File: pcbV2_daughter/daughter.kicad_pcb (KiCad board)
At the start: 2 copper layers, 93.7 x 93.3 mm, 80 parts, among them J1 Conn_01x02_Female, J2 USB_C_Receptacle, J3 Conn_01x03_Male, J6 Conn_01x03_Male, Q1 Q_NMOS_GSD, SW1 SW_Push, SW10 SW_Push, SW11 SW_Push, SW12 SW_Push, SW13 SW_SPDT, SW14 SW_Push, SW15 SW_Push, SW16 SW_Push, SW17 SW_DIP_x03, SW2 SW_Push, SW3 SW_Push, SW4 SW_Push, SW5 SW_Push, SW6 SW_Push, SW7 SW_Push, SW8 SW_Push, SW9 SW_Push, U1 Teensy4.0, U2 Waveshare_OLED_RGB

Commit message: finished v1 of daughter board
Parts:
- removed C13, C14, C15, C16: 1000uF, Capacitor_SMD:C_1206_3216Metric_Pad1.42x1.75mm_HandSolder
- removed D1, D10, D11, D12, D2, D3, D4, D5, D6, D7, D8, D9: D, Diode_SMD:D_SOD-323_HandSoldering
- removed D13: LED, LED_SMD:LED_1206_3216Metric_Pad1.42x1.75mm_HandSolder
- removed D26, D27, D28, D29: WS2812B, LED_SMD:LED_WS2812B_PLCC4_5.0x5.0mm_P3.2mm
- removed J1: Conn_01x02_Female, Connector_PinHeader_2.00mm:PinHeader_1x02_P2.00mm_Vertical
- removed J2: USB_C_Receptacle, custom:USB_C_REDUCED_UJ31-CH-G2
- removed Q1: Q_NMOS_GSD, Package_TO_SOT_SMD:SOT-23
- removed R1: R, Resistor_SMD:R_1206_3216Metric_Pad1.42x1.75mm_HandSolder
- removed R2, R3: 10K, Resistor_SMD:R_1206_3216Metric_Pad1.42x1.75mm_HandSolder
- removed R4: R_SHIELD, Resistor_SMD:R_1206_3216Metric_Pad1.42x1.75mm_HandSolder
- removed R6: JUMPER, Resistor_SMD:R_1206_3216Metric_Pad1.42x1.75mm_HandSolder
- removed the REF** at (163.6, 106.8)
- removed the REF** at (78.7, 106.8)
- removed the REF** at (121.2, 125.0)
- removed SW1, SW10, SW11, SW12, SW2, SW3, SW4, SW5, SW6, SW7, SW8, SW9: SW_Push, keyswitches:Kailh_socket_MX
- removed SW13: SW_SPDT, Connector_PinHeader_2.54mm:PinHeader_1x03_P2.54mm_Vertical
- removed SW14, SW15, SW16: SW_Push, custom:BTN_B3S-1000P
- removed SW17: SW_DIP_x03, custom:DIP3_219-3MSTR
- removed U1: Teensy4.0, teensy:Teensy40_REDUCED_PINS
- removed U2: Waveshare_OLED_RGB, Connector_PinHeader_2.54mm:PinHeader_1x07_P2.54mm_Vertical
- C1, C10, C11, C12, C2, C3, C4, C5, C6, C7, C8, C9, R5: moved to B.Cu
- J3, J6: moved to F.Cu
- moved R5 142.6 mm to (83.1, 122.9), turned to 180 degrees
- moved C1 142.3 mm to (91.4, 182.6), turned to 270 degrees
- moved C4 140.9 mm to (89.8, 123.2), turned to 270 degrees
- moved C3 137.3 mm to (89.7, 143.0), turned to 270 degrees
- moved C8 136.8 mm to (111.3, 182.7), turned to 90 degrees
- moved C2 131.4 mm to (91.4, 162.8), turned to 270 degrees
- moved C7 126.4 mm to (131.1, 182.6), turned to 270 degrees
- moved C6 122.0 mm to (111.1, 162.8)
- moved C5 114.2 mm to (130.9, 162.8), turned to 270 degrees
- moved C12 99.9 mm to (150.9, 182.6), turned to 90 degrees
- moved C11 93.7 mm to (150.9, 162.7), turned to 90 degrees
- moved C10 70.5 mm to (152.5, 143.0)
- moved C9 66.7 mm to (152.4, 123.2), turned to 90 degrees
- turned D20 to 180 degrees
- turned D21 to 180 degrees
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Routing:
- net +5V: track 0.00 -> 302.4 mm, vias 0 -> 12
- net Net-(D14-Pad4): track 0.00 -> 35.3 mm
- net Net-(D18-Pad4): track 0.00 -> 34.5 mm
- net Net-(D15-Pad4): track 0.00 -> 33.8 mm
- net Net-(D16-Pad4): track 0.00 -> 33.7 mm
- net Net-(D24-Pad4): track 0.00 -> 33.1 mm
- net Net-(D23-Pad4): track 0.00 -> 31.1 mm
- net Net-(D20-Pad4): track 0.00 -> 30.9 mm
- net Net-(D22-Pad4): track 0.00 -> 30.7 mm
- net GND: track 0.00 -> 30.0 mm, vias 0 -> 12
- net Net-(D18-Pad2): track 0.00 -> 21.8 mm
- net Net-(D14-Pad2): track 0.00 -> 21.4 mm
- net Net-(D19-Pad4): track 0.00 -> 21.0 mm
- net RGB_DOUT: track 0.00 -> 9.37 mm
- net Net-(D17-Pad4): track 0.00 -> 8.25 mm, vias 0 -> 1
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- added copper zone on B.Cu, net GND
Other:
- board size 93.7 x 93.3 mm -> 92.5 x 75.4 mm
- net class Trace_edge added: clearance 0.25, trace_width 0.25, via_dia 0.8, via_drill 0.4

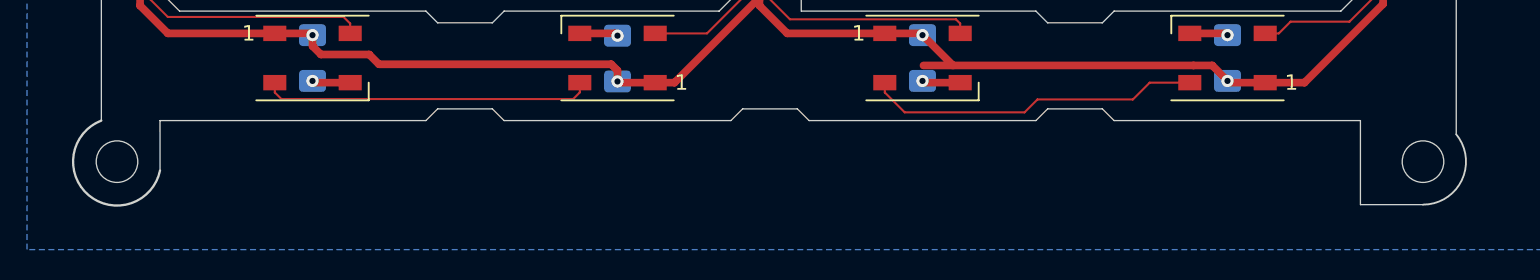
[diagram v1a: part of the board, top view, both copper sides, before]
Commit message: edited layout, updated daughter board
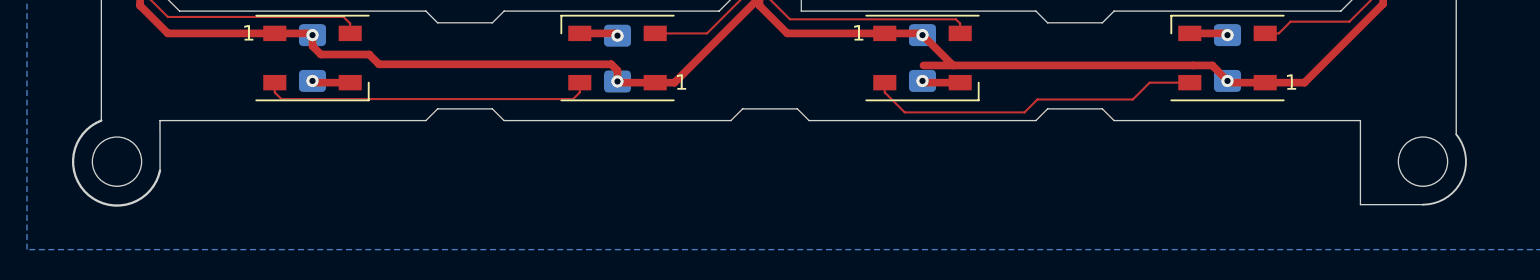
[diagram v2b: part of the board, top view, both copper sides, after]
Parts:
- removed the REF** at (78.7, 189.4)
- removed the REF** at (163.6, 189.4)
- added REF**: MountingHole_3.2mm_M3, MountingHole:MountingHole_3.2mm_M3, F.Cu at (78.7, 189.4)
- added REF**: MountingHole_3.2mm_M3, MountingHole:MountingHole_3.2mm_M3, F.Cu at (163.6, 189.4)
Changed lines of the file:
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@@
   (general
     (thickness 1.6)
-    (drawings 105)
+    (drawings 104)
     (tracks 236)
     (zones 0)
@@
   )
   (setup
-    (last_trace_width 0.5)
+    (last_trace_width 0.25)
     (user_trace_width 0.135)
     (user_trace_width 0.2)
@@
     (uvia_drill 0.1)
   )
-  (module MountingHole:MountingHole_2.7mm_M2.5 (layer F.Cu)
+  (module MountingHole:MountingHole_3.2mm_M3 (layer F.Cu)
     (at 78.74 189.357)
-    (descr "Mounting Hole 2.7mm, no annular, M2.5")
-    (tags "mounting hole 2.7mm no annular m2.5")
+    (descr "Mounting Hole 3.2mm, no annular, M3")
+    (tags "mounting hole 3.2mm no annular m3")
     (attr virtual)
-    (fp_text reference REF** (at 0 -3.7) (layer F.SilkS) hide
-      (effects (font (size 1 1) (thickness 0.15)))
-    )
-    (fp_text value MountingHole_2.7mm_M2.5 (at 0 3.7) (layer F.Fab)
-      (effects (font (size 1 1) (thickness 0.15)))
-    )
-    (fp_circle (center 0 0) (end 2.95 0) (layer F.CrtYd) (width 0.05))
-    (fp_circle (center 0 0) (end 2.7 0) (layer Cmts.User) (width 0.15))
+    (fp_text reference REF** (at 0 -4.2) (layer F.SilkS) hide
+      (effects (font (size 1 1) (thickness 0.15)))
+    )
+    (fp_text value MountingHole_3.2mm_M3 (at 0 4.2) (layer F.Fab)
+      (effects (font (size 1 1) (thickness 0.15)))
+    )
     (fp_text user %R (at 0.3 0) (layer F.Fab)
       (effects (font (size 1 1) (thickness 0.15)))
     )
-    (pad 1 np_thru_hole circle (at 0 0) (size 2.7 2.7) (drill 2.7) (layers *.Cu *.Mask))
-  )
-  (module MountingHole:MountingHole_2.7mm_M2.5 (layer F.Cu)
+    (fp_circle (center 0 0) (end 3.2 0) (layer Cmts.User) (width 0.15))
+    (fp_circle (center 0 0) (end 3.45 0) (layer F.CrtYd) (width 0.05))
+    (pad 1 np_thru_hole circle (at 0 0) (size 3.2 3.2) (drill 3.2) (layers *.Cu *.Mask))
+  )
+  (module MountingHole:MountingHole_3.2mm_M3 (layer F.Cu)
     (at 163.576 189.357)
-    (descr "Mounting Hole 2.7mm, no annular, M2.5")
-    (tags "mounting hole 2.7mm no annular m2.5")
+    (descr "Mounting Hole 3.2mm, no annular, M3")
+    (tags "mounting hole 3.2mm no annular m3")
     (attr virtual)
-    (fp_text reference REF** (at 0 -3.7) (layer F.SilkS) hide
-      (effects (font (size 1 1) (thickness 0.15)))
-    )
-    (fp_text value MountingHole_2.7mm_M2.5 (at 0 3.7) (layer F.Fab)
-      (effects (font (size 1 1) (thickness 0.15)))
-    )
-    (fp_circle (center 0 0) (end 2.95 0) (layer F.CrtYd) (width 0.05))
-    (fp_circle (center 0 0) (end 2.7 0) (layer Cmts.User) (width 0.15))
+    (fp_text reference REF** (at 0 -4.2) (layer F.SilkS) hide
+      (effects (font (size 1 1) (thickness 0.15)))
+    )
+    (fp_text value MountingHole_3.2mm_M3 (at 0 4.2) (layer F.Fab)
+      (effects (font (size 1 1) (thickness 0.15)))
+    )
+    (fp_circle (center 0 0) (end 3.45 0) (layer F.CrtYd) (width 0.05))
+    (fp_circle (center 0 0) (end 3.2 0) (layer Cmts.User) (width 0.15))
     (fp_text user %R (at 0.3 0) (layer F.Fab)
       (effects (font (size 1 1) (thickness 0.15)))
     )
-    (pad 1 np_thru_hole circle (at 0 0) (size 2.7 2.7) (drill 2.7) (layers *.Cu *.Mask))
+    (pad 1 np_thru_hole circle (at 0 0) (size 3.2 3.2) (drill 3.2) (layers *.Cu *.Mask))
   )
   (module Resistor_SMD:R_1206_3216Metric_Pad1.42x1.75mm_HandSolder (layer B.Cu)
@@
   (gr_line (start 82.804 117.094) (end 82.804 118.872) (layer Edge.Cuts) (width 0.05))
   (gr_line (start 74.93 117.094) (end 82.804 117.094) (layer Edge.Cuts) (width 0.05))
-  (gr_line (start 163.576 192.151) (end 159.512 192.151) (layer B.SilkS) (width 0.12))
   (gr_arc (start 163.576 189.357) (end 163.576 192.151) (angle -129.5) (layer Edge.Cuts) (width 0.12))
   (gr_arc (start 78.74 189.357) (end 77.724001 186.690001) (angle -237.6) (layer Edge.Cuts) (width 0.15))

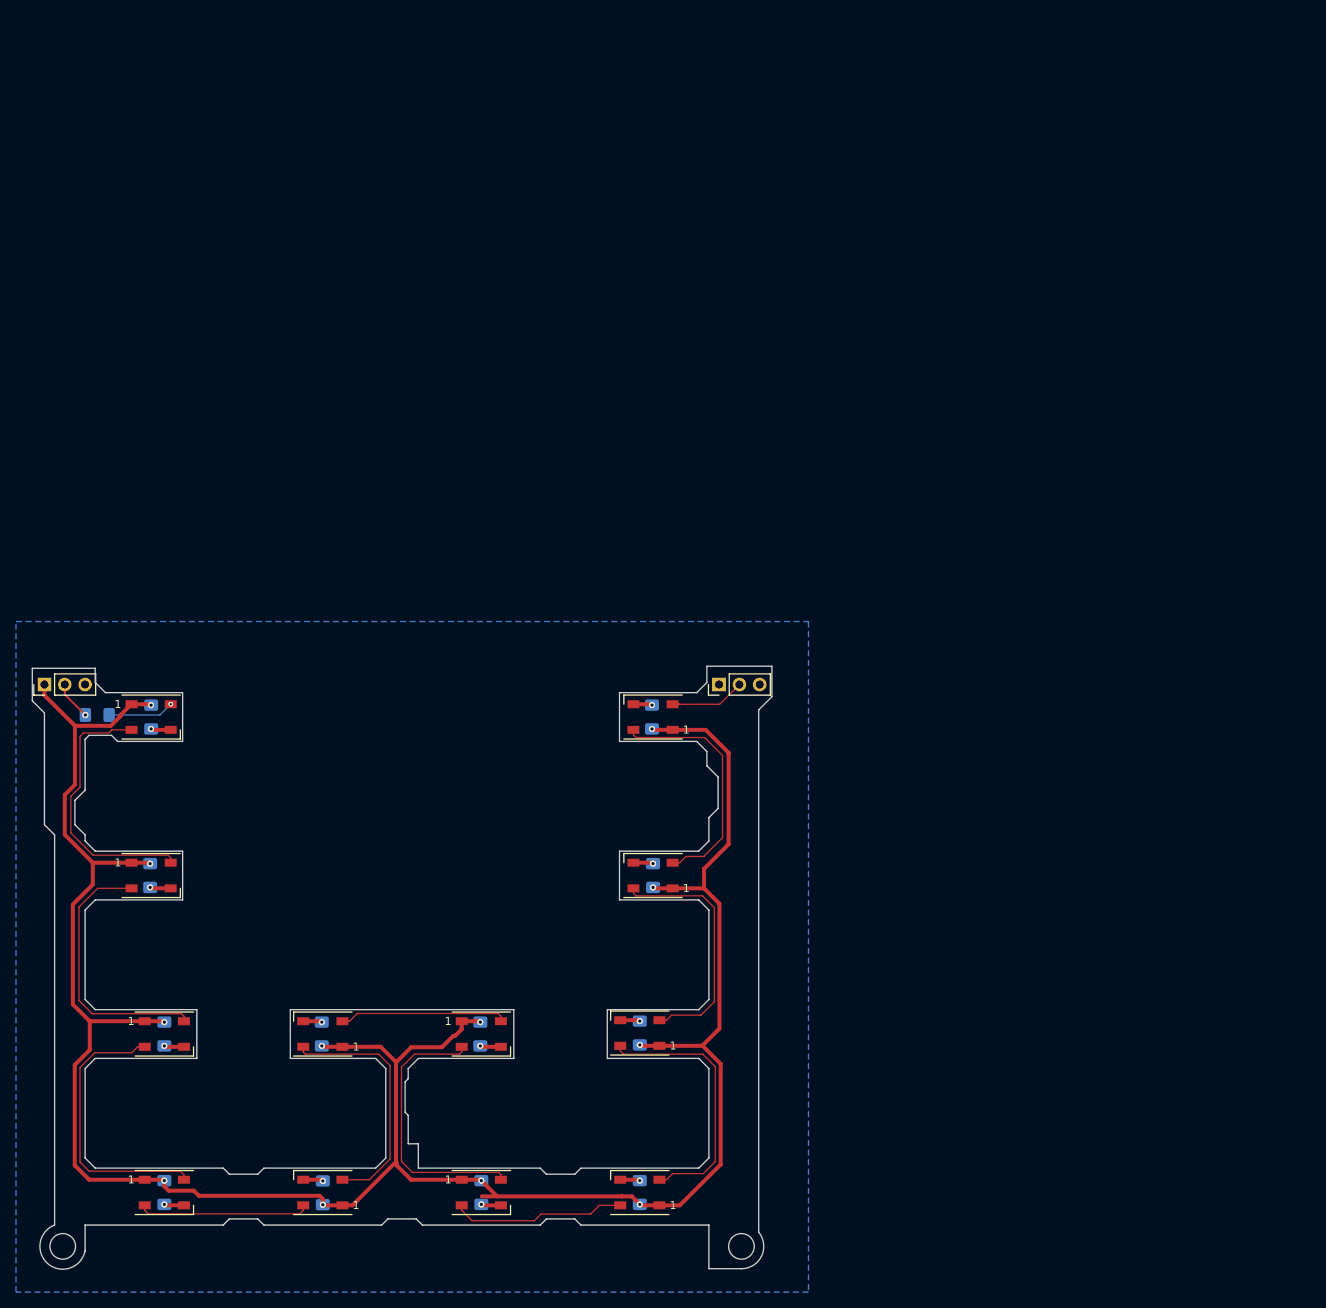
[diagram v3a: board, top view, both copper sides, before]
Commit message: updating daughter board to be more structurally safe
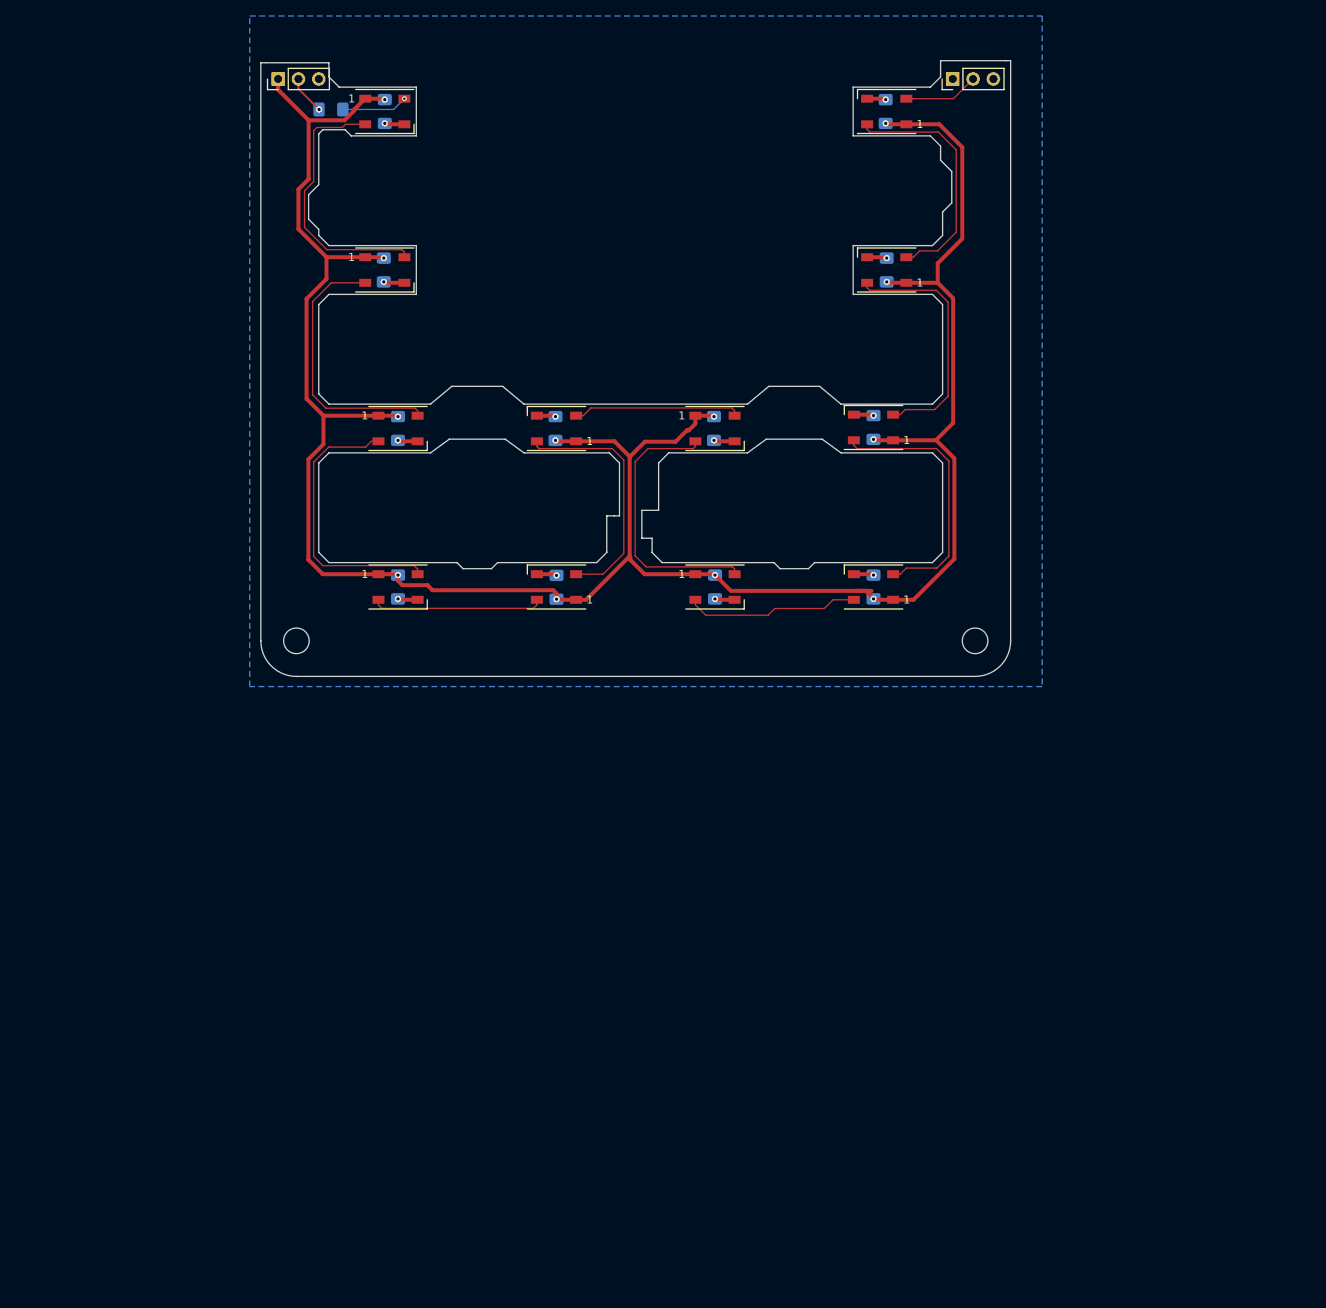
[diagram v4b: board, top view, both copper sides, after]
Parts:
- moved C1 81.1 mm to (120.7, 106.9)
- moved C10 81.1 mm to (181.7, 67.3)
- moved C11 81.1 mm to (180.1, 87.0)
- moved C12 81.1 mm to (180.1, 106.9)
- moved C3 81.1 mm to (118.9, 67.3)
- moved C4 81.1 mm to (119.0, 47.5)
- moved C7 81.1 mm to (160.3, 106.9)
- moved C9 81.1 mm to (181.6, 47.5)
- moved D14 81.1 mm to (120.7, 106.9)
- moved D16 81.1 mm to (119.0, 67.3)
- moved D17 81.1 mm to (119.0, 47.5)
- moved D18 81.1 mm to (160.3, 106.9)
- moved D21 81.1 mm to (140.5, 106.9)
- moved D22 81.1 mm to (181.7, 47.5)
- moved D23 81.1 mm to (181.7, 67.3)
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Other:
- board size 92.5 x 75.4 mm -> 93.7 x 77 mm
